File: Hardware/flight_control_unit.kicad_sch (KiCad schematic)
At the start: 36 parts, among them SW3 SW_SPDT, SW4 SW_Push_Dual, U12 STM32F405RGTx, Y2 25MHz

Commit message: pin refatoration, freertos code
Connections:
- net FCU_SDIO_DET: now also U12.40 (PC9); no longer U12.55 (PB3)
- net FCU_SP1_FLASH_CS: now also U12.20 (PA4); no longer U12.24 (PC4)
- net FCU_TIM2_CH1: now reaches U12.50 (PA15)
- net FCU_GPIOG: no longer names the net of U12.2 (PC13)
- net FCU_TIM1_CH1: no longer names the net of U12.41 (PA8)
- net FCU_TIM1_CH3 renamed FCU_USB_OTG_FS_ID
- new net FCU_TIM2_CH2: U12.55 (PB3)

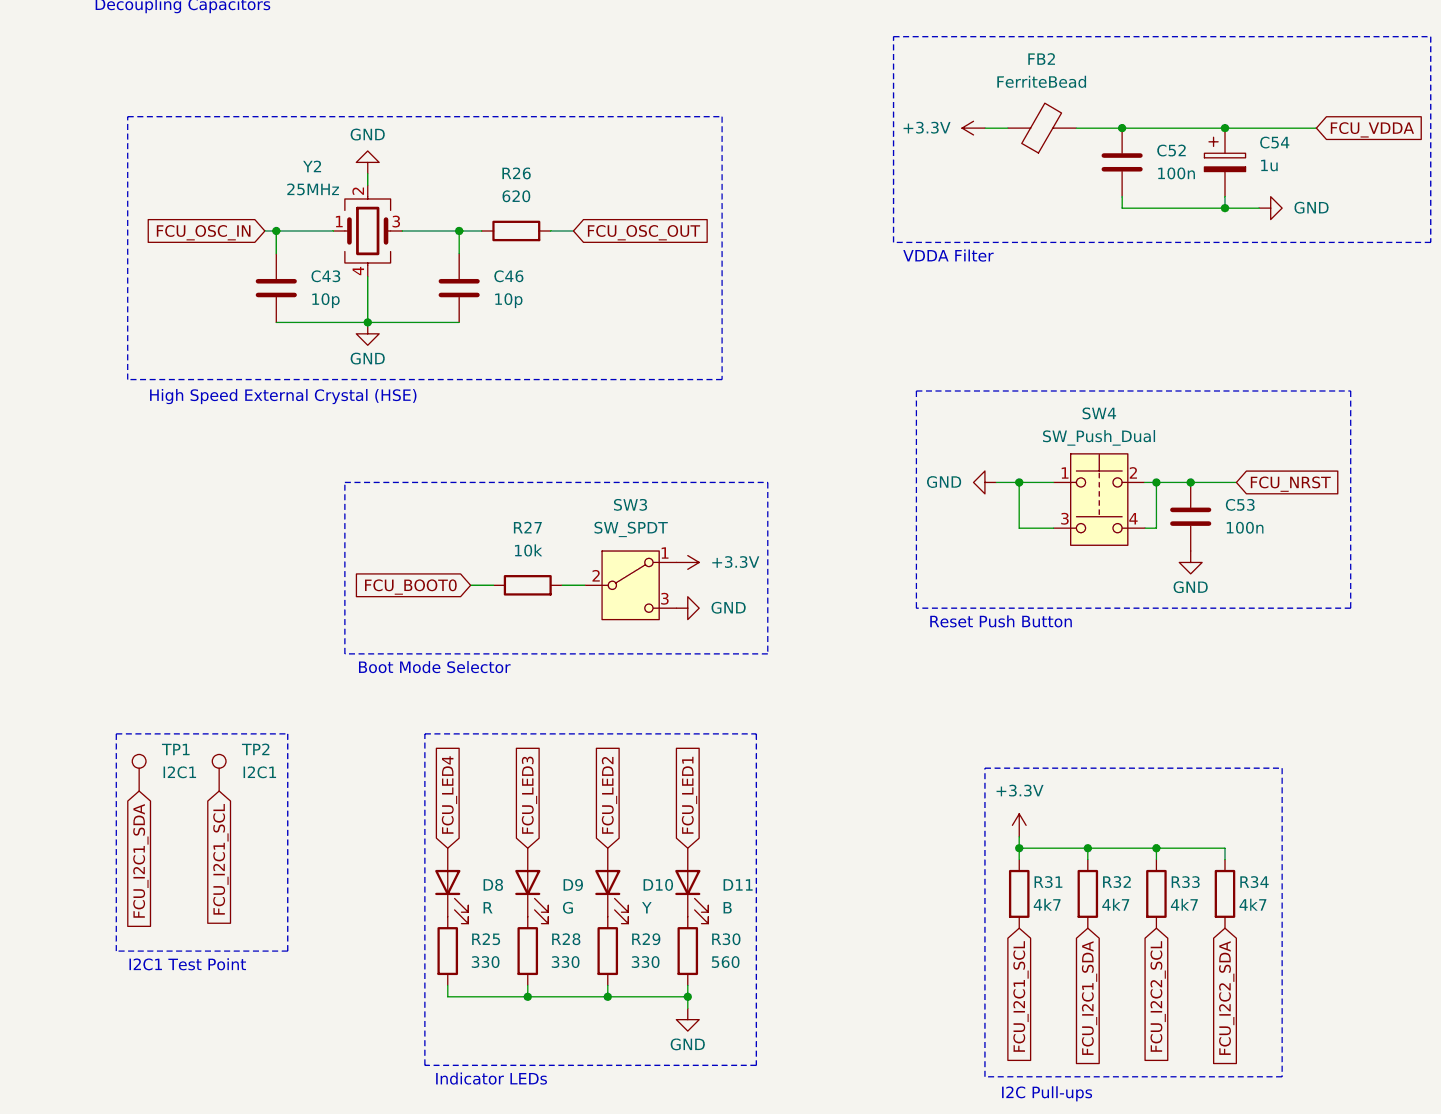
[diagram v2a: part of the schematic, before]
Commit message: add some footprints, and pcb configs
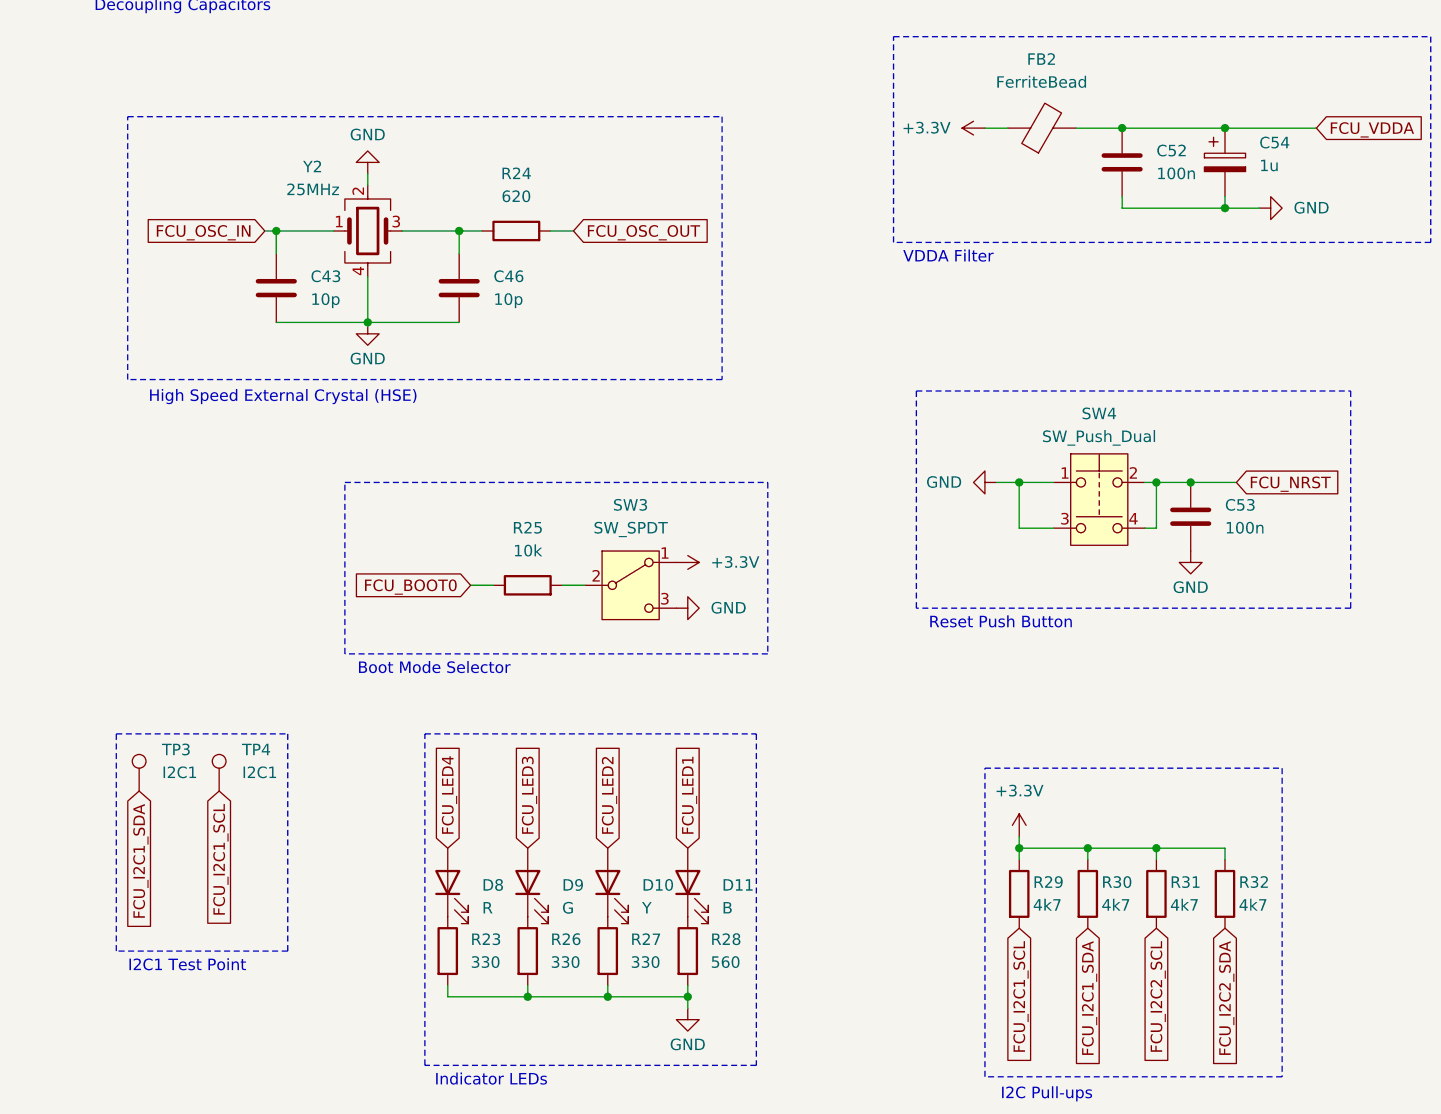
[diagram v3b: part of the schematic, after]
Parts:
- C40, C41, C53: footprint (none) -> Capacitor_SMD:C_0603_1608Metric
- C42, C54: footprint (none) -> Capacitor_Tantalum_SMD:CP_EIA-1608-08_AVX-J
- C43, C44, C45, C46, C47, C48, C49, C50, C51, C52: footprint (none) -> Capacitor_SMD:C_0402_1005Metric
- D10, D11, D8, D9: footprint (none) -> LED_SMD:LED_0805_2012Metric
- FB2: footprint (none) -> Inductor_SMD:L_0805_2012Metric
- R23: renamed from R25; footprint (none) -> Resistor_SMD:R_0603_1608Metric_Pad0.98x0.95mm_HandSolder
- R24: renamed from R26; footprint (none) -> Resistor_SMD:R_0603_1608Metric_Pad0.98x0.95mm_HandSolder
- R25: renamed from R27; footprint (none) -> Resistor_SMD:R_0603_1608Metric_Pad0.98x0.95mm_HandSolder
- R26: renamed from R28; footprint (none) -> Resistor_SMD:R_0603_1608Metric_Pad0.98x0.95mm_HandSolder
- R27: renamed from R29; footprint (none) -> Resistor_SMD:R_0603_1608Metric_Pad0.98x0.95mm_HandSolder
- R28: renamed from R30; footprint (none) -> Resistor_SMD:R_0603_1608Metric_Pad0.98x0.95mm_HandSolder
- R29: renamed from R31; footprint (none) -> Resistor_SMD:R_0603_1608Metric_Pad0.98x0.95mm_HandSolder
- R30: renamed from R32; footprint (none) -> Resistor_SMD:R_0603_1608Metric_Pad0.98x0.95mm_HandSolder
- R31: renamed from R33; footprint (none) -> Resistor_SMD:R_0603_1608Metric_Pad0.98x0.95mm_HandSolder
- R32: renamed from R34; footprint (none) -> Resistor_SMD:R_0603_1608Metric_Pad0.98x0.95mm_HandSolder
- TP3: renamed from TP1; footprint (none) -> TestPoint:TestPoint_Pad_D2.5mm
- TP4: renamed from TP2; footprint (none) -> TestPoint:TestPoint_Pad_D2.5mm
